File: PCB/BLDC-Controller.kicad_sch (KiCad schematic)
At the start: 79 parts, among them J1 Mot_Con_A, J2 Mot_Con_B, J3 Mot_Con_C, J4 Prog, J5 Receiver, J6 Bat_In, Q1 P75NF75, Q2 P75NF75, Q3 P75NF75, Q4 P75NF75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

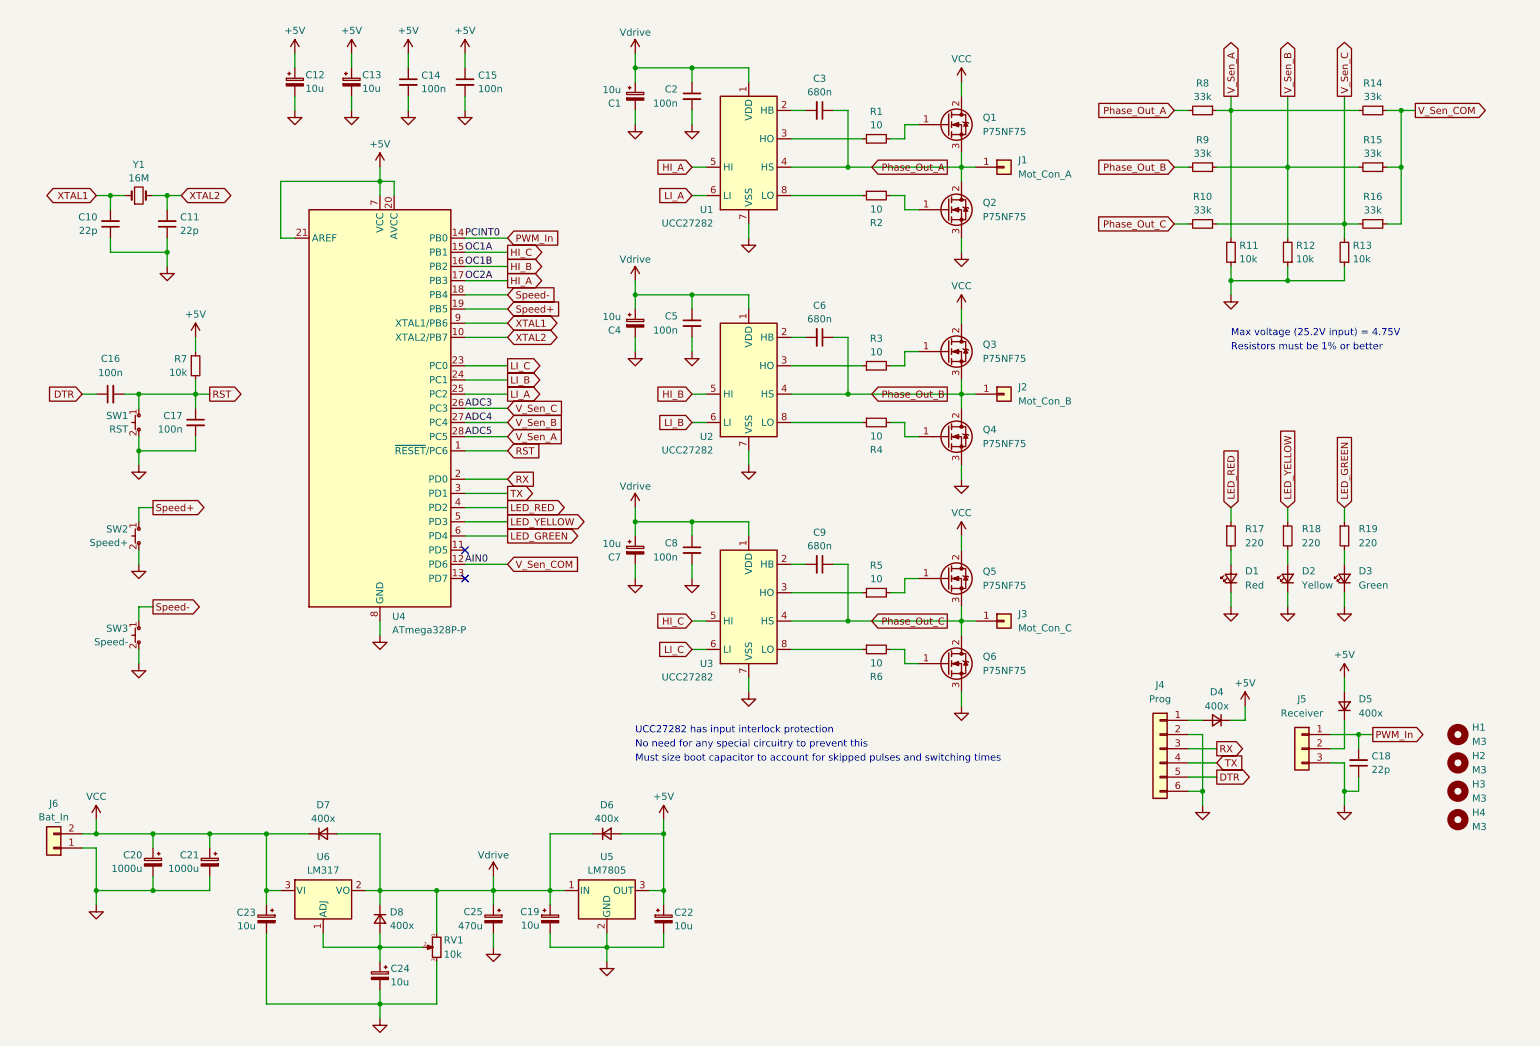
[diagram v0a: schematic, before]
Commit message: Uploaded images on system operation. Updated schematic.
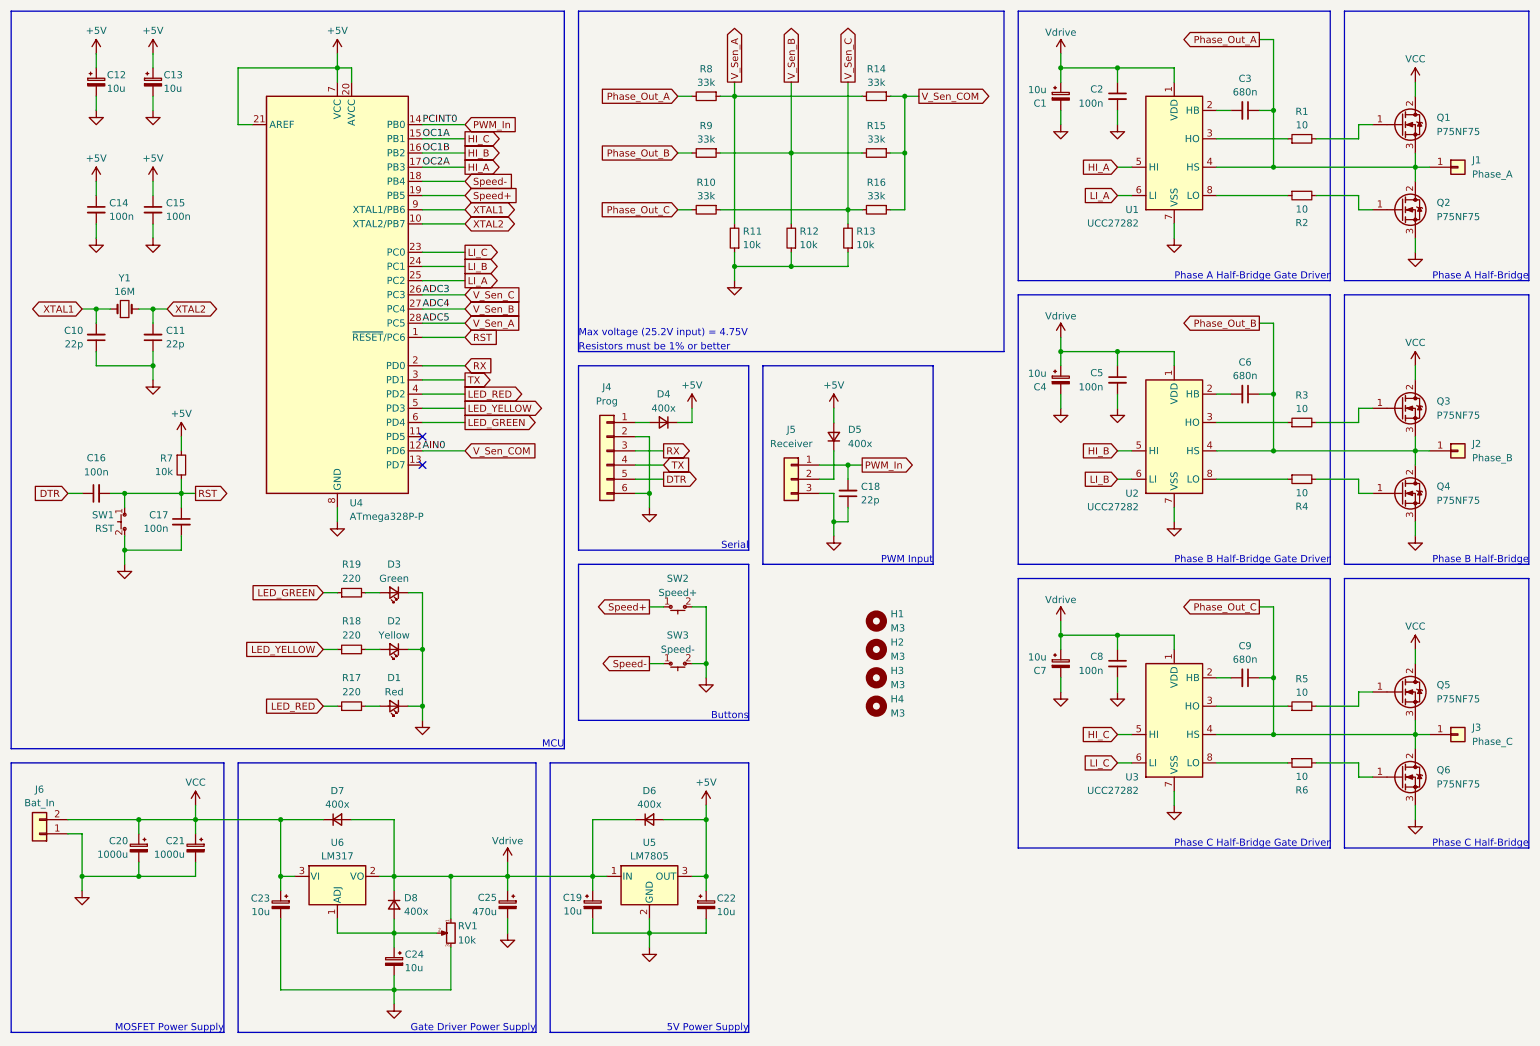
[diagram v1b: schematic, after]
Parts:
- J1: value Mot_Con_A -> Phase_A
- J2: value Mot_Con_B -> Phase_B
- J3: value Mot_Con_C -> Phase_C
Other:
- note added: "5V Power Supply"
- note added: "Buttons"
- note added: "Gate Driver Power Supply"
- note added: "MCU"
- note added: "MOSFET Power Supply"
- note added: "PWM Input"
- note added: "Phase A Half-Bridge"
- note added: "Phase A Half-Bridge Gate Driver"
- note added: "Phase B Half-Bridge"
- note added: "Phase B Half-Bridge Gate Driver"
- note added: "Phase C Half-Bridge"
- note added: "Phase C Half-Bridge Gate Driver"
- note added: "Serial"
- note removed: "Must size boot capacitor to account for skipped pulses and switching times"
- note removed: "No need for any special circuitry to prevent this"
- note removed: "UCC27282 has input interlock protection"
- moved on the sheet: C1, C10, C11, C12, C13, C14, C15, C16, C17, C18, C19, C2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

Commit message: Updated schematic.
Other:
- note added: "Zero-Crossing Detection Network"
- moved on the sheet: C20, C21, J6
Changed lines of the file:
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@@
   (junction (at 60.96 167.64) (diameter 0) (color 0 0 0 0)
   )
-  (junction (at 35.56 157.48) (diameter 0) (color 0 0 0 0)
+  (junction (at 35.56 167.64) (diameter 0) (color 0 0 0 0)
   )
   (junction (at 38.1 66.04) (diameter 0) (color 0 0 0 0)
@@
   (junction (at 127 177.8) (diameter 0) (color 0 0 0 0)
   )
-  (junction (at 45.72 157.48) (diameter 0) (color 0 0 0 0)
+  (junction (at 45.72 167.64) (diameter 0) (color 0 0 0 0)
   )
   (junction (at 162.56 93.98) (diameter 0) (color 0 0 0 0)
@@
   (junction (at 238.76 30.48) (diameter 0) (color 0 0 0 0)
   )
-  (junction (at 35.56 167.64) (diameter 0) (color 0 0 0 0)
+  (junction (at 35.56 177.8) (diameter 0) (color 0 0 0 0)
   )
   (junction (at 101.6 167.64) (diameter 0) (color 0 0 0 0)
@@
   (junction (at 137.16 129.54) (diameter 0) (color 0 0 0 0)
   )
-  (junction (at 60.96 157.48) (diameter 0) (color 0 0 0 0)
-  )
   (junction (at 238.76 40.64) (diameter 0) (color 0 0 0 0)
   )
   (junction (at 200.66 124.46) (diameter 0) (color 0 0 0 0)
   )
-  (junction (at 25.4 167.64) (diameter 0) (color 0 0 0 0)
+  (junction (at 25.4 177.8) (diameter 0) (color 0 0 0 0)
   )
   (junction (at 162.56 48.26) (diameter 0) (color 0 0 0 0)
@@
     (stroke (width 0) (type default))
   )
-  (wire (pts (xy 35.56 157.48) (xy 35.56 160.02))
+  (wire (pts (xy 35.56 167.64) (xy 35.56 170.18))
     (stroke (width 0) (type default))
   )
@@
     (stroke (width 0) (type default))
   )
-  (wire (pts (xy 25.4 167.64) (xy 25.4 160.02))
+  (wire (pts (xy 25.4 177.8) (xy 25.4 170.18))
     (stroke (width 0) (type default))
   )
@@
     (stroke (width 0) (type default))
   )
-  (wire (pts (xy 35.56 165.1) (xy 35.56 167.64))
+  (wire (pts (xy 35.56 175.26) (xy 35.56 177.8))
     (stroke (width 0) (type default))
   )
@@
     (stroke (width 0) (type default))
   )
-  (wire (pts (xy 22.86 160.02) (xy 25.4 160.02))
+  (wire (pts (xy 22.86 170.18) (xy 25.4 170.18))
     (stroke (width 0) (type default))
   )
@@
     (stroke (width 0) (type default))
   )
-  (wire (pts (xy 35.56 167.64) (xy 45.72 167.64))
+  (wire (pts (xy 35.56 177.8) (xy 45.72 177.8))
     (stroke (width 0) (type default))
   )
@@
     (stroke (width 0) (type default))
   )
-  (wire (pts (xy 60.96 157.48) (xy 60.96 167.64))
-    (stroke (width 0) (type default))
-  )
   (wire (pts (xy 127 177.8) (xy 127 180.34))
     (stroke (width 0) (type default))
@@
     (stroke (width 0) (type default))
   )
-  (wire (pts (xy 45.72 157.48) (xy 45.72 160.02))
+  (wire (pts (xy 45.72 167.64) (xy 45.72 170.18))
     (stroke (width 0) (type default))
   )
@@
     (stroke (width 0) (type default))
   )
-  (wire (pts (xy 25.4 170.18) (xy 25.4 167.64))
+  (wire (pts (xy 25.4 180.34) (xy 25.4 177.8))
     (stroke (width 0) (type default))
   )
@@
     (stroke (width 0) (type default))
   )
-  (wire (pts (xy 25.4 167.64) (xy 35.56 167.64))
+  (wire (pts (xy 25.4 177.8) (xy 35.56 177.8))
     (stroke (width 0) (type default))
   )
@@
     (stroke (width 0) (type default))
   )
-  (wire (pts (xy 45.72 154.94) (xy 45.72 157.48))
+  (wire (pts (xy 45.72 165.1) (xy 45.72 167.64))
     (stroke (width 0) (type default))
   )
-  (wire (pts (xy 22.86 157.48) (xy 35.56 157.48))
+  (wire (pts (xy 22.86 167.64) (xy 35.56 167.64))
     (stroke (width 0) (type default))
   )
@@
     (stroke (width 0) (type default))
   )
-  (wire (pts (xy 45.72 157.48) (xy 60.96 157.48))
+  (wire (pts (xy 45.72 167.64) (xy 60.96 167.64))
     (stroke (width 0) (type default))
   )
@@
     (stroke (width 0) (type default))
   )
-  (wire (pts (xy 45.72 157.48) (xy 35.56 157.48))
+  (wire (pts (xy 45.72 167.64) (xy 35.56 167.64))
     (stroke (width 0) (type default))
   )
@@
     (stroke (width 0) (type default))
   )
-  (wire (pts (xy 45.72 167.64) (xy 45.72 165.1))
+  (wire (pts (xy 45.72 177.8) (xy 45.72 175.26))
     (stroke (width 0) (type default))
   )
@@
     (stroke (width 0) (type default))
   )
+  (wire (pts (xy 60.96 167.64) (xy 60.96 157.48))
+    (stroke (width 0) (type default))
+  )
   (wire (pts (xy 60.96 175.26) (xy 60.96 187.96))
     (stroke (width 0) (type default))
@@
     (effects (font (size 1.27 1.27)) (justify right bottom))
   )
+  (text "Zero-Crossing Detection Network" (at 190.5 73.66 0)
+    (effects (font (size 1.27 1.27)) (justify right bottom))
+  )
   (text "Phase C Half-Bridge Gate Driver" (at 248.92 162.56 0)
     (effects (font (size 1.27 1.27)) (justify right bottom))
@@
     )
   )
-  (symbol (lib_id "Device:C_Polarized_Small") (at 45.72 162.56 0) (mirror y) (unit 1)
+  (symbol (lib_id "Device:C_Polarized_Small") (at 45.72 172.72 0) (mirror y) (unit 1)
     (in_bom yes) (on_board yes) (dnp no)
-    (property "Reference" "C21" (at 43.815 161.29 0)
+    (property "Reference" "C21" (at 43.815 171.45 0)
       (effects (font (size 1.27 1.27)) (justify left))
     )
-    (property "Value" "1000u" (at 43.815 163.7142 0)
+    (property "Value" "1000u" (at 43.815 173.8742 0)
       (effects (font (size 1.27 1.27)) (justify left))
     )
-    (property "Footprint" "Ariamelon-Device:CP_Radial_D16.0mm_P7.62mm" (at 45.72 162.56 0)
+    (property "Footprint" "Ariamelon-Device:CP_Radial_D16.0mm_P7.62mm" (at 45.72 172.72 0)
       (effects (font (size 1.27 1.27)) hide)
     )
-    (property "Datasheet" "~" (at 45.72 162.56 0)
+    (property "Datasheet" "~" (at 45.72 172.72 0)
       (effects (font (size 1.27 1.27)) hide)
     )
@@
     )
   )
-  (symbol (lib_id "Connector_Generic:Conn_01x02") (at 17.78 160.02 180) (unit 1)
+  (symbol (lib_id "Connector_Generic:Conn_01x02") (at 17.78 170.18 180) (unit 1)
     (in_bom yes) (on_board yes) (dnp no) (fields_autoplaced)
-    (property "Reference" "J6" (at 17.78 152.0657 0)
+    (property "Reference" "J6" (at 17.78 162.2257 0)
       (effects (font (size 1.27 1.27)))
     )
-    (property "Value" "Bat_In" (at 17.78 154.4899 0)
+    (property "Value" "Bat_In" (at 17.78 164.6499 0)
       (effects (font (size 1.27 1.27)))
     )
-    (property "Footprint" "Connector_AMASS:AMASS_XT60-M_1x02_P7.20mm_Vertical" (at 17.78 160.02 0)
+    (property "Footprint" "Connector_AMASS:AMASS_XT60-M_1x02_P7.20mm_Vertical" (at 17.78 170.18 0)
       (effects (font (size 1.27 1.27)) hide)
     )
-    (property "Datasheet" "~" (at 17.78 160.02 0)
+    (property "Datasheet" "~" (at 17.78 170.18 0)
       (effects (font (size 1.27 1.27)) hide)
     )
@@
     )
   )
-  (symbol (lib_id "Device:C_Polarized_Small") (at 35.56 162.56 0) (mirror y) (unit 1)
+  (symbol (lib_id "Device:C_Polarized_Small") (at 35.56 172.72 0) (mirror y) (unit 1)
     (in_bom yes) (on_board yes) (dnp no)
-    (property "Reference" "C20" (at 33.655 161.29 0)
+    (property "Reference" "C20" (at 33.655 171.45 0)
       (effects (font (size 1.27 1.27)) (justify left))
     )
-    (property "Value" "1000u" (at 33.655 163.7142 0)
+    (property "Value" "1000u" (at 33.655 173.8742 0)
       (effects (font (size 1.27 1.27)) (justify left))
     )
-    (property "Footprint" "Ariamelon-Device:CP_Radial_D16.0mm_P7.62mm" (at 35.56 162.56 0)
+    (property "Footprint" "Ariamelon-Device:CP_Radial_D16.0mm_P7.62mm" (at 35.56 172.72 0)
       (effects (font (size 1.27 1.27)) hide)
     )
-    (property "Datasheet" "~" (at 35.56 162.56 0)
+    (property "Datasheet" "~" (at 35.56 172.72 0)
       (effects (font (size 1.27 1.27)) hide)
     )
@@
     )
   )
-  (symbol (lib_id "power:VCC") (at 45.72 154.94 0) (unit 1)
+  (symbol (lib_id "power:VCC") (at 45.72 165.1 0) (unit 1)
     (in_bom yes) (on_board yes) (dnp no) (fields_autoplaced)
-    (property "Reference" "#PWR024" (at 45.72 158.75 0)
+    (property "Reference" "#PWR024" (at 45.72 168.91 0)
       (effects (font (size 1.27 1.27)) hide)
     )
-    (property "Value" "VCC" (at 45.72 150.8069 0)
+    (property "Value" "VCC" (at 45.72 160.9669 0)
       (effects (font (size 1.27 1.27)))
     )
-    (property "Footprint" "" (at 45.72 154.94 0)
+    (property "Footprint" "" (at 45.72 165.1 0)
       (effects (font (size 1.27 1.27)) hide)
     )
-    (property "Datasheet" "" (at 45.72 154.94 0)
+    (property "Datasheet" "" (at 45.72 165.1 0)
       (effects (font (size 1.27 1.27)) hide)
     )
@@
     )
   )
-  (symbol (lib_id "power:GND") (at 25.4 170.18 0) (mirror y) (unit 1)
+  (symbol (lib_id "power:GND") (at 25.4 180.34 0) (mirror y) (unit 1)
     (in_bom yes) (on_board yes) (dnp no) (fields_autoplaced)
-    (property "Reference" "#PWR0121" (at 25.4 176.53 0)
+    (property "Reference" "#PWR0121" (at 25.4 186.69 0)
       (effects (font (size 1.27 1.27)) hide)
     )
-    (property "Value" "GND" (at 25.4 173.99 0)
+    (property "Value" "GND" (at 25.4 184.15 0)
       (effects (font (size 1.27 1.27)) hide)
     )
-    (property "Footprint" "" (at 25.4 170.18 0)
+    (property "Footprint" "" (at 25.4 180.34 0)
       (effects (font (size 1.27 1.27)) hide)
     )
-    (property "Datasheet" "" (at 25.4 170.18 0)
+    (property "Datasheet" "" (at 25.4 180.34 0)
       (effects (font (size 1.27 1.27)) hide)
     )
